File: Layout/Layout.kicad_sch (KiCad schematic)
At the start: 0 parts

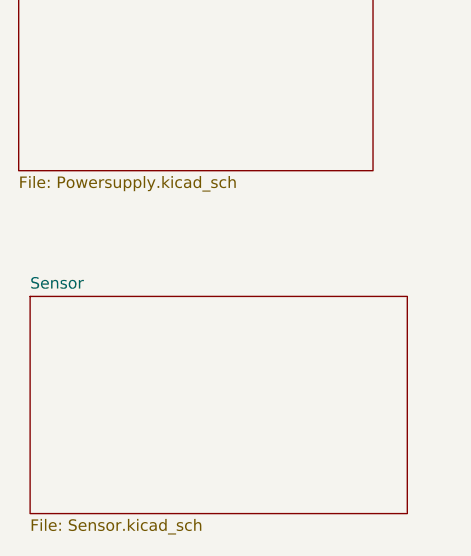
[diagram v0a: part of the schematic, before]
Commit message: First ICs Placed$
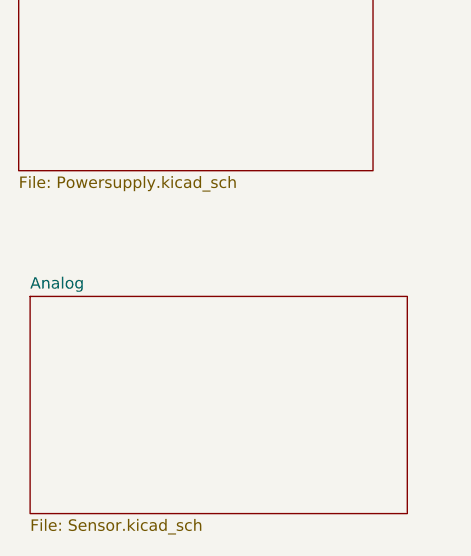
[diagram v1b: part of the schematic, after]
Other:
- sheet Sensor renamed Analog
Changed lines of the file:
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@@
 			(color 0 0 0 0.0000)
 		)
-		(property "Sheetname" "Sensor"
+		(property "Sheetname" "Analog"
 			(at 46.99 118.6684 0)
 			(effects

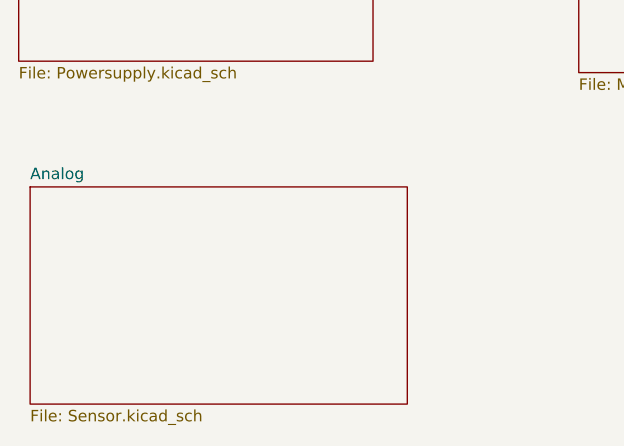
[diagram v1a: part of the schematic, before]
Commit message: Version with 3x VL53L4CD ToF sensors to calculate angle of measured plane
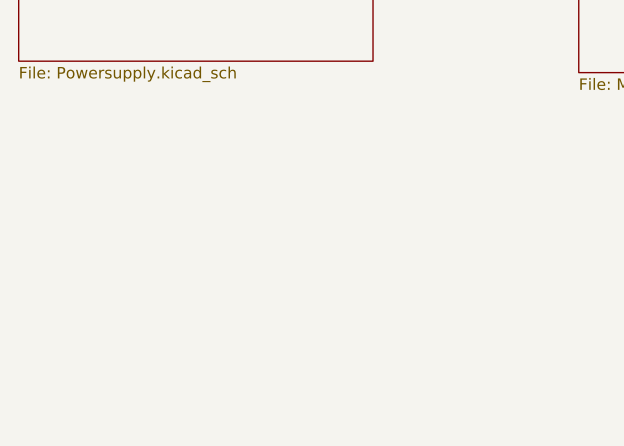
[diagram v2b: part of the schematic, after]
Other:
- removed sheet Analog
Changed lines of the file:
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@@
-	)
-	(sheet
-		(at 46.99 119.38)
-		(size 41.91 24.13)
-		(exclude_from_sim no)
-		(in_bom yes)
-		(on_board yes)
-		(dnp no)
-		(fields_autoplaced yes)
-		(stroke
-			(width 0.1524)
-			(type solid)
-		)
-		(fill
-			(color 0 0 0 0.0000)
-		)
-		(property "Sheetname" "Analog"
-			(at 46.99 118.6684 0)
-			(effects
-				(font
-					(size 1.27 1.27)
-				)
-				(justify left bottom)
-			)
-		)
-		(property "Sheetfile" "Sensor.kicad_sch"
-			(at 46.99 144.0946 0)
-			(effects
-				(font
-					(size 1.27 1.27)
-				)
-				(justify left top)
-			)
-		)
-		(instances
-			(project "Layout"
-				(path "/cdb7c10d-ec58-4b12-af63-2fb6474199a1"
-					(page "4")
-				)
-			)
-		)
 	)
 	(sheet

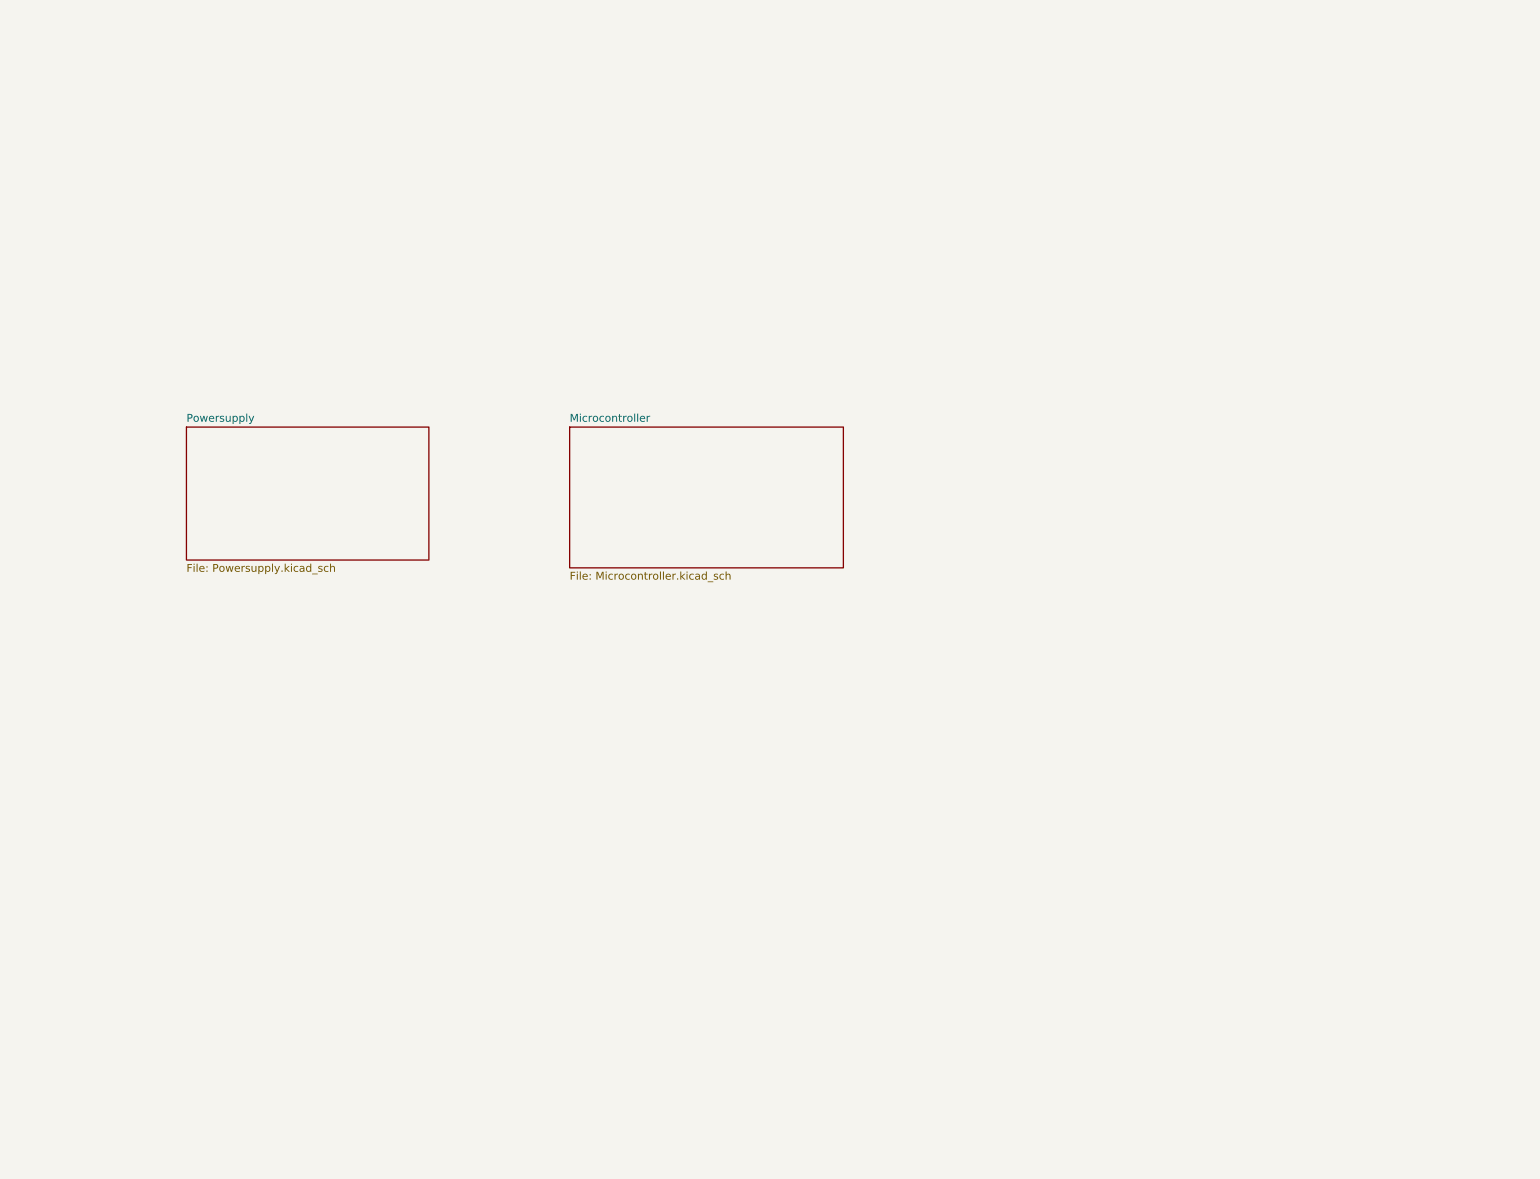
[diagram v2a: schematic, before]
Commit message: Added: Debugging LEDs Removed: 2x Tof Sensors Merged: All Schematic sheets
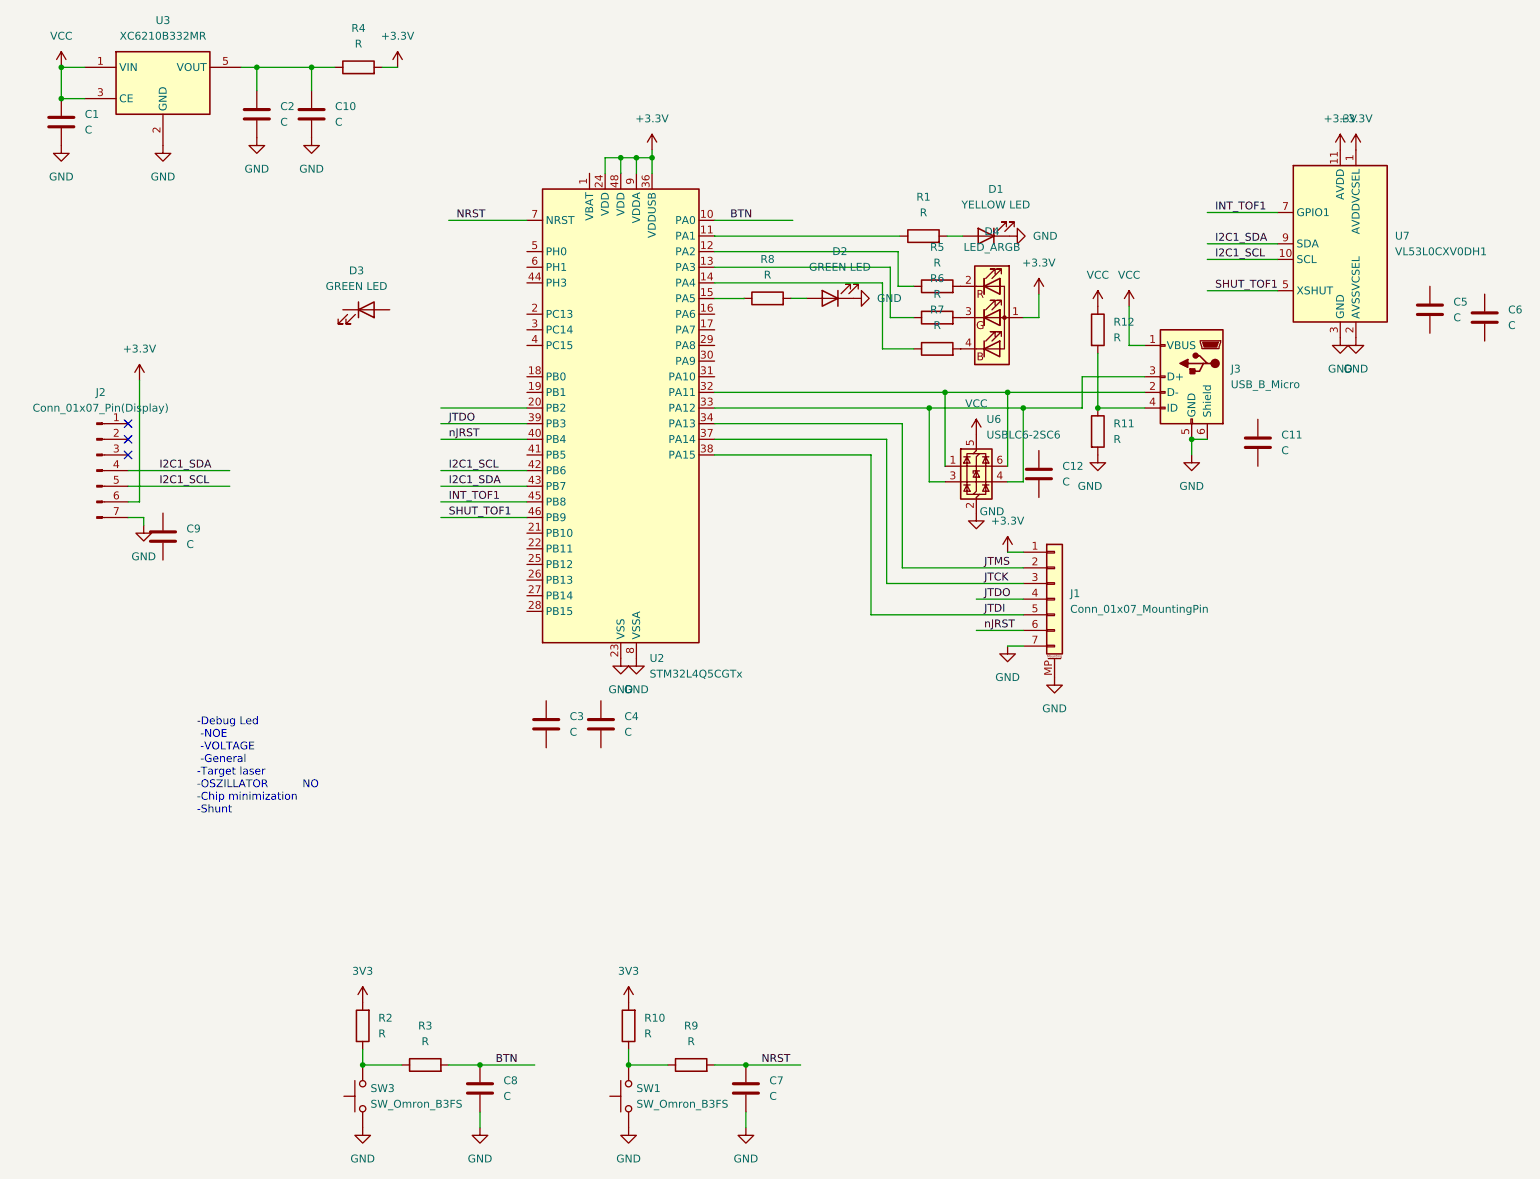
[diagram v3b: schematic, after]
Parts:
- added C1, C10, C11, C12, C2, C3, C4, C5, C6, C7, C8, C9: C, symbol Device:C
- added D1: YELLOW LED, symbol Device:LED
- added D2, D3: GREEN LED, symbol Device:LED
- added D4: LED_ARGB, symbol Device:LED_ARGB
- added J1: Conn_01x07_MountingPin, symbol Connector_Generic_MountingPin:Conn_01x07_MountingPin
- added J2: Conn_01x07_Pin(Display), symbol Connector:Conn_01x07_Pin
- added J3: USB_B_Micro, symbol Connector:USB_B_Micro
- added R1, R10, R11, R12, R2, R3, R4, R5, R6, R7, R8, R9: R, symbol Device:R
- added SW1, SW3: SW_Omron_B3FS, symbol Switch:SW_Omron_B3FS
- added U2: STM32L4Q5CGTx, Package_QFP:LQFP-48_7x7mm_P0.5mm, symbol MCU_ST_STM32L4:STM32L4Q5CGTx
- added U3: XC6210B332MR, Package_TO_SOT_SMD:SOT-23-5, symbol Regulator_Linear:XC6210B332MR
- added U6: USBLC6-2SC6, Package_TO_SOT_SMD:SOT-23-6, symbol Power_Protection:USBLC6-2SC6
- added U7: VL53L0CXV0DH1, Sensor_Distance:ST_VL53L1x, symbol Sensor_Distance:VL53L0CXV0DH1
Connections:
- new net: C10.1, C2.1, R4.1, U3.5 (VOUT)
- new net: D1.2 (A), R1.2
- new net: D4.2 (RK), R5.2
- new net: D4.3 (GK), R6.2
- new net: D4.4 (BK), R7.2
- new net: R1.1, U2.11 (PA1)
- new net: R5.1, U2.12 (PA2)
- new net: R2.1, R3.1, SW3.2
- new net: J3.4 (ID), R11.1, R12.2
- new net: R10.1, R9.1, SW1.2
- new net: R6.1, U2.13 (PA3)
- new net: R7.1, U2.14 (PA4)
- new net: R8.1, U2.15 (PA5)
- new net: J3.2 (D-), U2.32 (PA11), U6.1 (I/O1), U6.6 (I/O1)
- new net: J3.3 (D+), U2.33 (PA12), U6.3 (I/O2), U6.4 (I/O2)
- new net: D2.2 (A), R8.2
- new net +3.3V: D4.1 (A), J1.1 (Pin_1), J2.6 (Pin_6), R4.2, U2.24 (VDD), U2.36 (VDDUSB), U2.48 (VDD), U2.9 (VDDA), U7.1 (AVDDVCSEL), U7.11 (AVDD)
- new net 3V3: R10.2, R2.2
- new net BTN: C8.1, R3.2, U2.10 (PA0)
- new net GND: C1.2, C10.2, C2.2, C7.2, C8.2, D1.1 (K), D2.1 (K), J1.7 (Pin_7), J1.MP (MountPin), J2.7 (Pin_7), J3.5 (GND), J3.6 (Shield), R11.2, SW1.1, SW3.1, U2.23 (VSS), U2.35 (VSS), U2.47 (VSS), U2.8 (VSSA), U3.2 (GND), U6.2 (GND), U7.12 (GND), U7.2 (AVSSVCSEL), U7.3 (GND), U7.4 (GND), U7.6 (GND)
- new net I2C1_SCL: J2.5 (Pin_5), U2.42 (PB6), U7.10 (SCL)
- new net I2C1_SDA: J2.4 (Pin_4), U2.43 (PB7), U7.9 (SDA)
- new net INT_TOF1: U2.45 (PB8), U7.7 (GPIO1)
- new net JTCK: J1.3 (Pin_3), U2.37 (PA14)
- new net JTDI: J1.5 (Pin_5), U2.38 (PA15)
- new net JTDO: J1.4 (Pin_4), U2.39 (PB3)
- new net JTMS: J1.2 (Pin_2), U2.34 (PA13)
- new net NRST: C7.1, R9.2, U2.7 (NRST)
- new net SHUT_TOF1: U2.46 (PB9), U7.5 (XSHUT)
- new net VCC: C1.1, J3.1 (VBUS), R12.1, U3.1 (VIN), U3.3 (CE), U6.5 (VBUS)
- new net nJRST: J1.6 (Pin_6), U2.40 (PB4)
- no-connect marks 0 -> 3
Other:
- removed sheet Microcontroller
- removed sheet Powersupply
- note added: "-Debug Led -NOE -VOLTAGE -General -Target laser -OSZILLATOR NO -Chip minimization -Shunt"

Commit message: Dayum
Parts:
- removed D3: GREEN LED, symbol Device:LED
- removed D4: LED_ARGB, symbol Device:LED_ARGB
- removed J1: Conn_01x07_MountingPin, symbol Connector_Generic_MountingPin:Conn_01x07_MountingPin
- removed J2: Conn_01x07_Pin(Display), symbol Connector:Conn_01x07_Pin
- removed U2: STM32L4Q5CGTx, Package_QFP:LQFP-48_7x7mm_P0.5mm, symbol MCU_ST_STM32L4:STM32L4Q5CGTx
- removed U7: VL53L0CXV0DH1, Sensor_Distance:ST_VL53L1x, symbol Sensor_Distance:VL53L0CXV0DH1
- added C13: C, Capacitor_SMD:C_0603_1608Metric, symbol Device:C
- added C14: 10uF, Capacitor_SMD:C_0603_1608Metric, symbol Device:C
- added C15, C16, C17, C19: 100nF, Capacitor_SMD:C_0603_1608Metric, symbol Device:C
- added C18: n/a, Capacitor_SMD:C_0603_1608Metric, symbol Device:C
- added D3: RLD65NZN5-00A, Laser:RLD65NZN500A, symbol RLD65NZN5-00A:RLD65NZN5-00A
- added D4, D5: BLUE LED, LED_SMD:LED_0603_1608Metric, symbol Device:LED
- added G1: Laser_Warnschild, Laser:Laser_Warnschild, symbol RLD65NZN5-00A:Laser_Warnschild
- added IC1: VL53L4CDV0DH_1, VL53L4CDV0DH/1:VL53L4CDV0DH1, symbol VL53L4CDV0DH_1:VL53L4CDV0DH_1
- added IC2: MAX4231AUT+T, Package_TO_SOT_SMD:SOT-23-6, symbol MAX4231AUT+T:MAX4231AUT+T
- added J1: Conn_01x07_Pin, Connector_PinHeader_2.54mm:PinHeader_1x07_P2.54mm_Vertical_SMD_Pin1Left, symbol Connector:Conn_01x07_Pin
- added R13: R, Resistor_SMD:R_0603_1608Metric, symbol Device:R
- added R14: 0R, Resistor_SMD:R_0603_1608Metric, symbol Device:R
- added R15: 0R, symbol Device:R
- added R16: 4.7k, Resistor_SMD:R_0603_1608Metric, symbol Device:R
- added R18, R19: n/a, Resistor_SMD:R_0603_1608Metric, symbol Device:R
- added RN1: 100R 4x0603, Resistor_SMD:R_Array_Concave_4x0603, symbol Device:R_Pack04
- added TR1: 2N7002AQ-7, Package_TO_SOT_SMD:SOT-23-3, symbol 2026-10-10_22-11-14:2N7002AQ-7
- added U2: AD8293G160ARJZ-R7, Package_TO_SOT_SMD:SOT-23-8, symbol 2026-10-10_13-37-23:AD8293G160ARJZ-R7
- added U4: ~, Package_TO_SOT_SMD:SOT-23-6, symbol 2026-10-10_13-37-23:R1580N001A-TR-FE
- added U5: STM32F042G6Ux, Package_DFN_QFN:QFN-28_4x4mm_P0.5mm, symbol STM32F042G4U6:STM32F042G6Ux
- added Y1: SG-210STF_48.0000ML5, Oszi:SG210STF480000ML5, symbol SG-210STF_48_0000ML5:SG-210STF_48.0000ML5
- C1, C2: value C -> 1uF; footprint (none) -> Capacitor_SMD:C_0603_1608Metric
- C10, C12, C3, C4, C5, C6, C7, C8, C9: value C -> 100nF; footprint (none) -> Capacitor_SMD:C_0603_1608Metric
- C11: value C -> n/a; footprint (none) -> Capacitor_SMD:C_0603_1608Metric
- D1: footprint (none) -> LED_SMD:LED_0603_1608Metric
- D2: value GREEN LED -> BLUE LED; footprint (none) -> LED_SMD:LED_0603_1608Metric
- R1: value R -> 330R; footprint (none) -> Resistor_SMD:R_0603_1608Metric
- R10, R2, R3, R9: value R -> 10k; footprint (none) -> Resistor_SMD:R_0603_1608Metric
- R11, R12: value R -> n/a; footprint (none) -> Resistor_SMD:R_0603_1608Metric
- R4: value R -> 0R; footprint (none) -> Resistor_SMD:R_0603_1608Metric
- R5, R6, R7: value R -> 390R; footprint (none) -> Resistor_SMD:R_0603_1608Metric
- R8: value R -> 0R
- SW1, SW3: footprint (none) -> Button_Switch_SMD:SW_SPST_B3S-1000
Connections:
- net 3V3 is gone; now on net +3.3V: R10.2, R2.2
- net +3.3V: now also C3.1, C4.1, C5.1, C6.1, C9.1, C14.1, C15.1, C17.1, IC1.1 (AVDDVCSEL_1), IC1.11 (AVDD), IC1.13 (AVDDVCSEL_2), IC2.6 (VDD), J1.6 (Pin_6), R18.1, R19.1, U2.3 (REF), U2.7 (VS+), U4.4 (VIN), U5.17 (VDD), U5.18 (VDDIO2), U5.5 (VDDA), Y1.4 (VCC)
- net BTN: now also U5.6 (PA0)
- net GND: now also C11.1, C12.2, C3.2, C4.2, C5.2, C6.2, C9.2, R8.2, C14.2, C15.2, C16.2, C17.2, C18.1, C19.2, D3.3 (A_LD/K_PD), D4.1 (K), D5.1 (K), IC1.12 (GND4), IC1.2 (AVSSVCSEL), IC1.3 (GND), IC1.4 (GND2), IC1.6 (GND3), IC2.1 (IN+), IC2.2 (VSS), J1.7 (Pin_7), R13.2, RN1.1 (R1.1), RN1.2 (R2.1), RN1.3 (R3.1), RN1.4 (R4.1), TR1.3 (D), U2.2 (GND), U4.5 (GND), U5.16 (VSSA), Y1.2 (GND); no longer J3.5 (GND), J3.6 (Shield)
- net I2C1_SCL: now also IC1.10 (SCL), J1.5 (Pin_5), R19.2, U5.1 (PB8)
- net I2C1_SDA: now also IC1.9 (SDA), J1.4 (Pin_4), R18.2, U5.28 (PB7)
- net INT_TOF1: now also IC1.7 (GPIO1), U5.26 (PB5)
- net NRST: now also U5.4 (NRST)
- net SHUT_TOF1: now also IC1.5 (XSHUT), U5.23 (PA15)
- net VCC: no longer C1.1, J3.1 (VBUS), R12.1, U3.1 (VIN), U3.3 (CE)
- net at R5.2: now also D2.2 (A)
- net at R6.2: now also D4.2 (A)
- net at R7.2: now also D5.2 (A)
- net LED_USB: now reaches R1.1
- net LED_USB: now also U5.7 (PA1)
- net LED_B1: now reaches R5.1
- net LED_B1: now also U5.10 (PA4)
- net +5V: now reaches C12.1
- net +5V: now also C1.1, J3.1 (VBUS), R12.1, U3.1 (VIN), U3.3 (CE), C19.1, R14.1
- net LED_B2: now reaches R6.1
- net LED_B2: now also U5.11 (PA5)
- net LED_B3: now reaches R7.1
- net LED_B3: now also U5.12 (PA6)
- net at R8.1: now also U2.1 (IN-)
- net USB_DM: now reaches J3.2 (D-), U6.1 (I/O1), U6.6 (I/O1)
- net USB_DM: now also U5.19 (PA9/PA11)
- net USB_DP: now reaches J3.3 (D+), U6.3 (I/O2), U6.4 (I/O2)
- net USB_DP: now also U5.20 (PA10/PA12)
- net U_SHUNT: now reaches C11.2
- net U_SHUNT: now also U2.4 (ADCOUT), U5.25 (PB4)
- new net: C13.1, U2.6 (OUT)
- new net: C13.2, U2.5 (FILT)
- new net: RN1.5 (R4.2), RN1.6 (R3.2), RN1.7 (R2.2), RN1.8 (R1.2), TR1.2 (S), U4.2 (SOURCE)
- new net: D3.1 (K_LD), R14.2
- new net: D3.2 (A_PD), IC2.3 (IN-), R16.1
- new net: C16.1, U4.1 (ISET)
- new net: TR1.1 (G), U4.3 (GATE)
- new net: R15.1, U2.8 (IN+)
- new net DIM_LASER: U4.6 (DIM)
- new net IN+_SHUNT: J3.5 (GND), R13.1, R15.2
- new net NSTBY_OSC: U5.3 (PF1), Y1.1 (~{ST})
- new net PD_LASER: C18.2, IC2.4 (OUT), R16.2, U5.24 (PB3)
- new net RCC_OSC_IN: U5.2 (PF0), Y1.3 (OUT)
- new net SYS_SWCLK: U5.22 (PA14)
- new net SYS_SWDIO: U5.21 (PA13)
- new net USART1_TX: U5.27 (PB6)
- no-connect marks 3 -> 11
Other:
- note added: "-Debug Led -NOE Done -VOLTAGE No need -General Done -Target laser Done -OSZILLATOR Done -Chip minimization Done -Shunt Done"
- note added: "f(U)=U/(160*R_SHUNT)= I_TOT"
- note added: "f(U)=U^2 * R = P_LASER"
- note removed: "-Debug Led -NOE -VOLTAGE -General -Target laser -OSZILLATOR NO -Chip minimization -Shunt"
- moved on the sheet: C1, C10, C2, C7, C8, C9, D1, J3, R1, R10, R11, R12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

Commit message: Started with Layout
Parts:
- removed C11: n/a, Capacitor_SMD:C_0603_1608Metric, symbol Device:C
- removed C4: 100nF, Capacitor_SMD:C_0603_1608Metric, symbol Device:C
- removed J3: USB_B_Micro, symbol Connector:USB_B_Micro
- removed U5: STM32F042G6Ux, Package_DFN_QFN:QFN-28_4x4mm_P0.5mm, symbol STM32F042G4U6:STM32F042G6Ux
- added IC3: STM32F042G4U6, uC:uC_Footprint, symbol STM32F042G4U6:STM32F042G4U6
- added J2: USB_B_Micro, Connector_USB:USB_Micro-B_Amphenol_10118193-0001LF_Horizontal, symbol Connector:USB_B_Micro
- added J3: Conn_01x03_Pin, Connector_PinHeader_2.54mm:PinHeader_1x03_P2.54mm_Vertical_SMD_Pin1Left, symbol Connector:Conn_01x03_Pin
- added J4: Conn_01x04_Pin, Connector_PinHeader_2.54mm:PinHeader_1x04_P2.54mm_Vertical_SMD_Pin1Left, symbol Connector:Conn_01x04_Pin
- C13: value C -> 47nF
- R13: value R -> shunt; footprint Resistor_SMD:R_0603_1608Metric -> Resistor_SMD:R_2512_6332Metric
- R15, R8: footprint (none) -> Resistor_SMD:R_0603_1608Metric
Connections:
- net VCC is gone; now on net +5V: U6.5 (VBUS)
- net +3.3V: now also IC3.17 (VDD), IC3.18 (VDDIO2), IC3.5 (VDDA), J4.1 (Pin_1)
- net +5V: now also J2.1 (VBUS)
- net BTN: now also IC3.6 (PA0)
- net DIM_LASER: now also IC3.15 (PB1)
- net GND: now also IC3.16 (VSSA), J3.3 (Pin_3), J4.3 (Pin_3)
- net I2C1_SCL: now also IC3.1 (PB8)
- net I2C1_SDA: now also IC3.28 (PB7)
- net IN+_SHUNT: now also J2.5 (GND)
- net INT_TOF1: now also IC3.26 (PB5)
- net LED_B1: now also IC3.10 (PA4)
- net LED_B2: now also IC3.11 (PA5)
- net LED_B3: now also IC3.12 (PA6)
- net LED_USB: now also IC3.7 (PA1)
- net NRST: now also IC3.4 (NRST)
- net NSTBY_OSC: now also IC3.3 (PF1)
- net PD_LASER: now also IC3.24 (PB3)
- net RCC_OSC_IN: now also IC3.2 (PF0)
- net SHUT_TOF1: now also IC3.23 (PA15)
- net SYS_SWCLK: now also IC3.22 (PA14), J4.2 (Pin_2)
- net SYS_SWDIO: now also IC3.21 (PA13), J4.4 (Pin_4)
- net USART1_TX: now also IC3.27 (PB6), J3.2 (Pin_2)
- net USB_DM: now also IC3.19 (PA9/PA11), J2.2 (D-)
- net USB_DP: now also IC3.20 (PA10/PA12), J2.3 (D+)
- net U_SHUNT: now also IC3.25 (PB4)
- net at R11.1, R12.2: now also J2.4 (ID)
- new net GPIO_PB0: IC3.14 (PB0), J3.1 (Pin_1)
- no-connect marks 11 -> 9

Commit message: Last commit before short Review of Master
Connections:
- net USB_DM renamed USB_D-
- net USB_DP renamed USB_D+
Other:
- note added: "Display Connection"
- note added: "Inst.Amp."
- note added: "Microcontroller"
- note added: "Oscillator"
- note added: "PC-Connection"
- note added: "Powersupply"
- note added: "Targeting Laser + Photo Diode"
- note added: "ToF Sensor"
- moved on the sheet: C12, C19, C9, G1, J1, J2, R11, R12, R13, R18, R19, U6
